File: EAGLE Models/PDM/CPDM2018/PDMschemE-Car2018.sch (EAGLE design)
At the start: 16 parts, among them Q1 PFETBS250

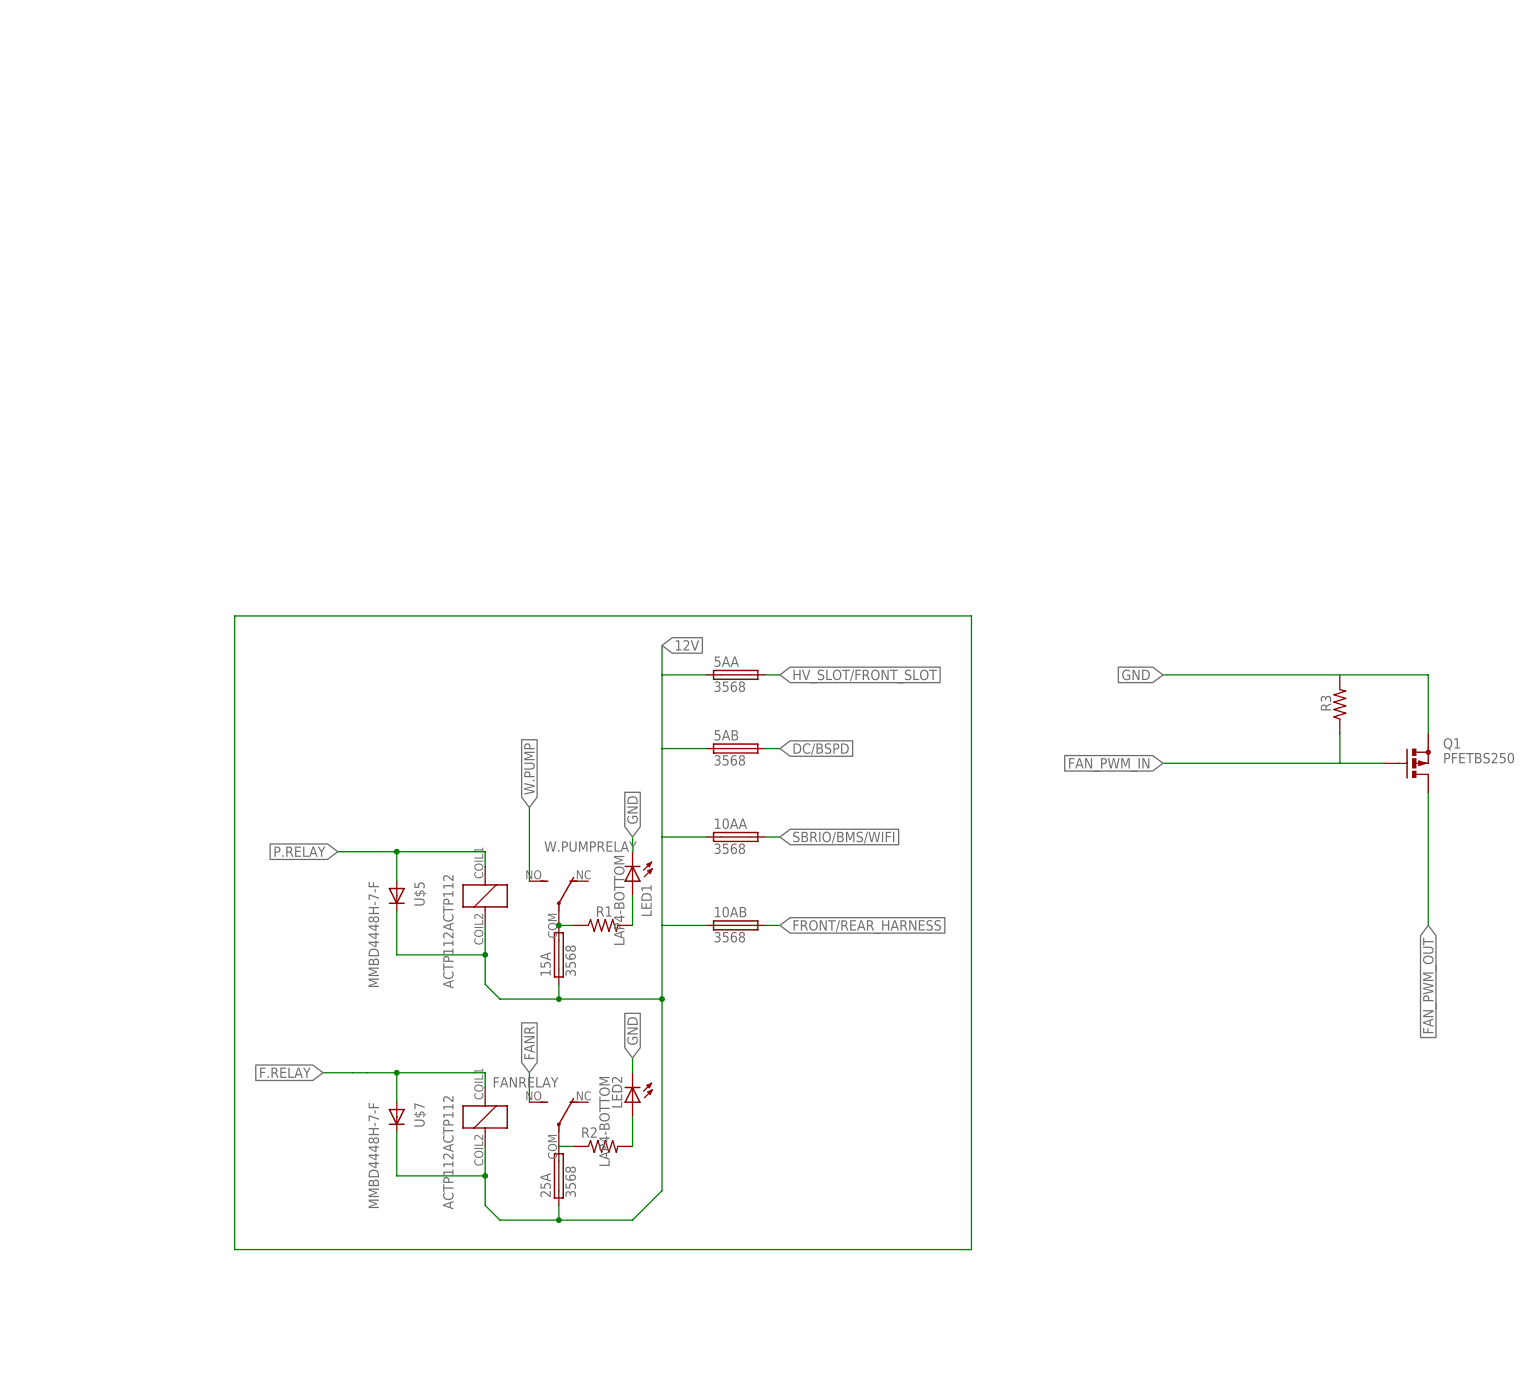
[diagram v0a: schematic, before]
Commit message: Organized PDM components
Organized PDM componenets into individualized boxes; Addded spacing for more readability
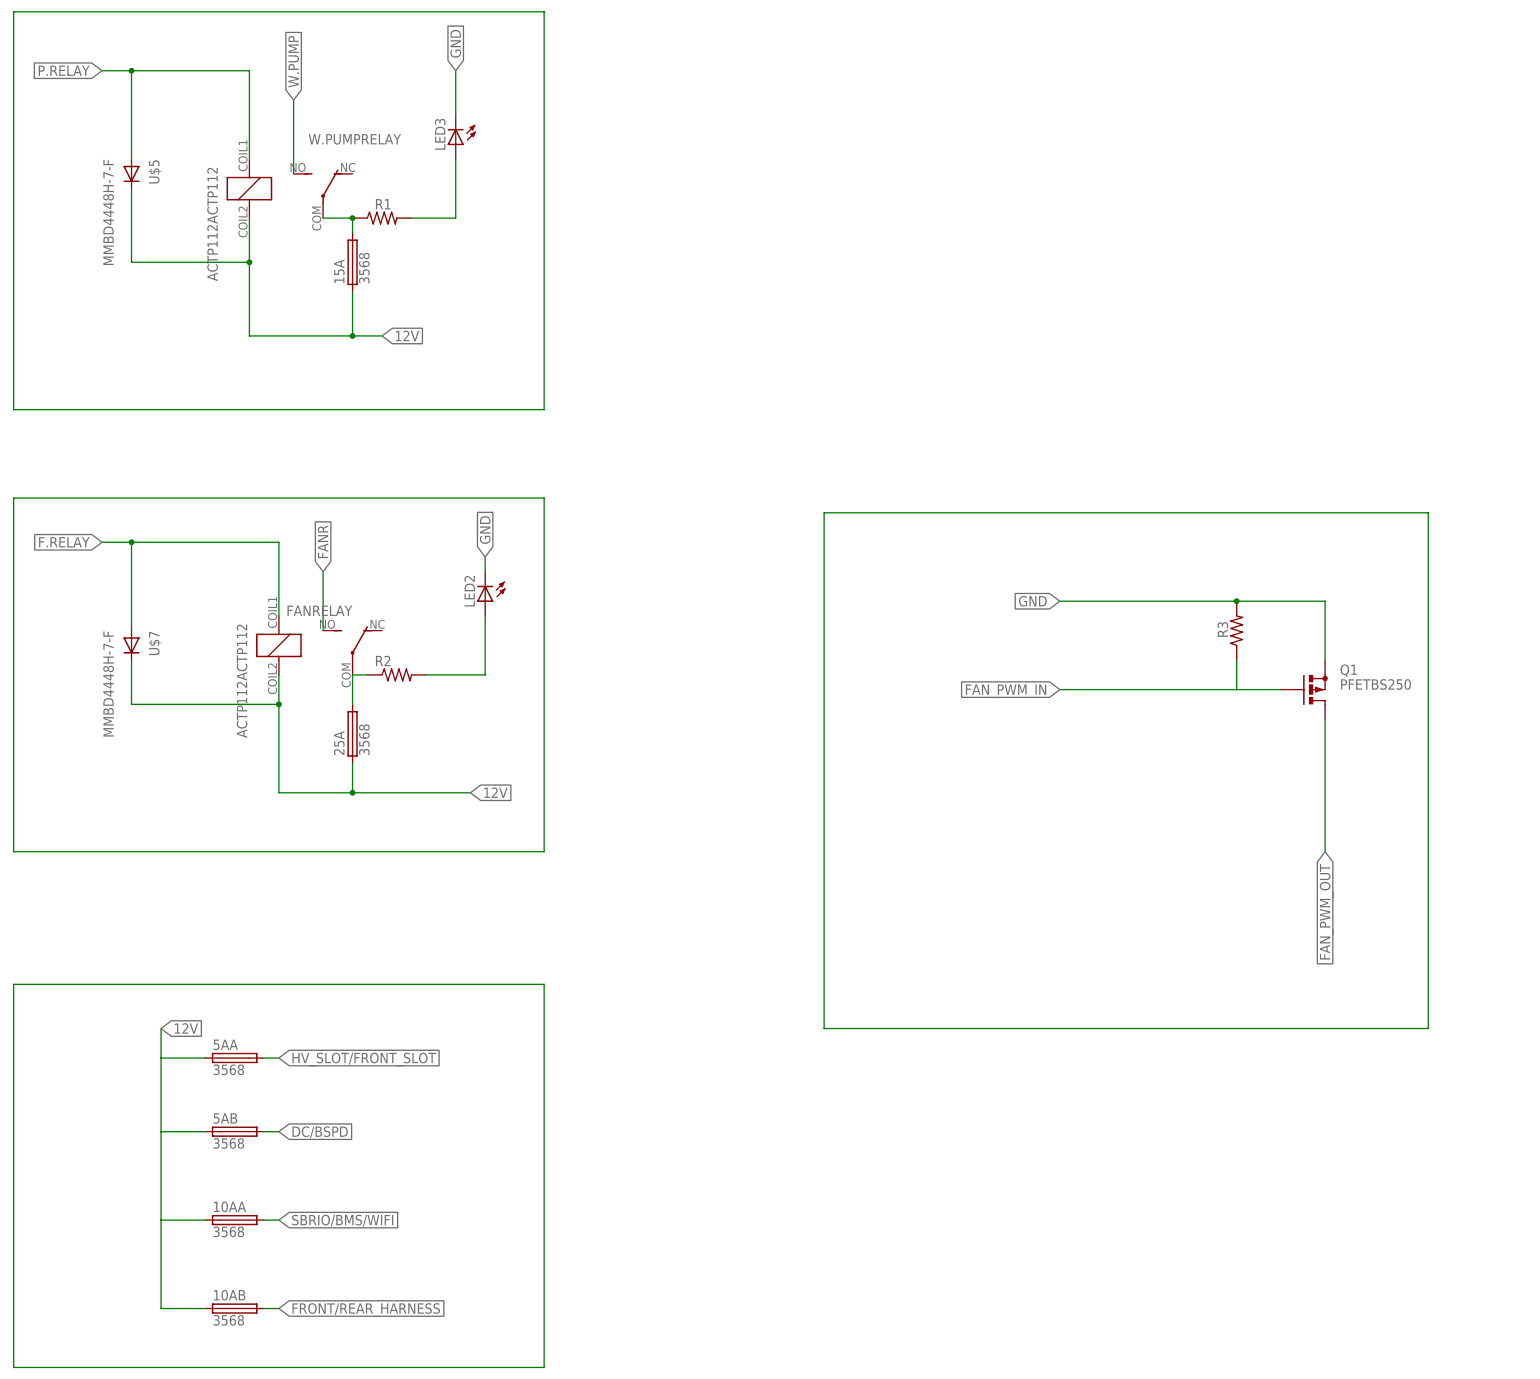
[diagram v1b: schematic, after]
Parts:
- removed LED1: LAP4-BOTTOM, led:LAP4-BOTTOM
- added LED3: (no value), adafruit:LEDCHIPLED_0805
- LED2: value LAP4-BOTTOM -> (none); device led:LAP4-BOTTOM -> adafruit:LEDCHIPLED_0805
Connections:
- net GND: now also LED3.C, R3.2; no longer LED1.C
- net N$1: now also LED3.A; no longer LED1.A
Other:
- moved on the sheet: 10AA, 10AB, 15A, 25A, 5AA, 5AB, FANRELAY, LED2, Q1, R1, R2, R3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

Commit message: E-Car PDM: Fuse Indicators added
The new type of blown fuse indicators were added. Organized circuit to be easier to read.
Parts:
- added D1, D2, D3, D4, D5, D6: 1N4004, adafruit:1N4004
- added LED1, LED4, LED5, LED6: (no value), adafruit:LEDCHIPLED_0805
- added Q2, Q3, Q4, Q5, Q6: 2N2907, adafruit:2N2907
- added R10, R12, R5, R6, R8: 47K, resistor:R-US_R1206
- added R11, R4, R7, R9: (no value), resistor:R-US_R1206
- added U$1: IRF40B207, infineon:IRF40B207
- Q1: value PFETBS250 -> 2N2907; device adafruit:PFETBS250 -> adafruit:2N2907
- R3: value (none) -> 47K
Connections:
- net FANR renamed FAN
- removed net FAN_PWM_IN: Q1.G, R3.1
- removed net FAN_PWM_OUT: Q1.D
- new net N$10: 15A.1, D1.A, W.PUMPRELAY.COM
- new net N$11: Q2.C, R4.1
- new net N$13: LED2.C, Q2.E
- new net N$14: D3.C, Q3.B, R6.1
- new net N$17: LED4.C, Q4.E
- new net N$18: D4.C, Q4.B, R8.1
- new net N$19: Q4.C, R7.1
- new net N$22: LED5.C, Q5.E
- new net N$23: D5.C, Q5.B, R10.1
- new net N$24: Q5.C, R9.1
- new net N$27: LED6.C, Q6.E
- new net N$28: D6.C, Q6.B, R12.1
- new net N$29: Q6.C, R11.1
- new net N$3: LED1.C, Q3.E
- new net N$5: Q1.C, R1.1
- net 12V: now also 10AA.2, 10AB.2, 15A.2, 25A.2, 5AA.2, 5AB.2, LED1.A, LED2.A, LED3.A, LED4.A, LED5.A, LED6.A; no longer 10AA.1, 10AB.1, 15A.1, 25A.1, 5AA.1, 5AB.1, FANRELAY.COIL2, U$5.C, U$7.C, W.PUMPRELAY.COIL2
- net DC/BSPD: now also 5AB.1, D4.A; no longer 5AB.2
- net F.RELAY: now also U$7.C; no longer U$7.A
- net FRONT/REAR_HARNESS: now also 10AB.1, D6.A; no longer 10AB.2
- net GND: now also FANRELAY.COIL2, R1.2, R10.2, R11.2, R12.2, R2.2, R4.2, R5.2, R6.2, R7.2, R8.2, R9.2, U$5.A, U$7.A, W.PUMPRELAY.COIL2; no longer LED2.C, LED3.C, Q1.S
- net HV_SLOT/FRONT_SLOT: now also 5AA.1, D3.A; no longer 5AA.2
- net N$1: now also LED3.C, Q1.E; no longer LED3.A, R1.2
- net N$2: now also Q3.C
- net N$4: now also 25A.1, D2.A, FANRELAY.COM; no longer LED2.A, R2.2
- net N$6: now also D1.C, Q1.B, R3.1; no longer 15A.2, R1.1, W.PUMPRELAY.COM
- net N$9: now also D2.C, Q2.B, R5.1; no longer 25A.2, FANRELAY.COM
- net P.RELAY: now also U$5.C; no longer U$5.A
- net SBRIO/BMS/WIFI: now also 10AA.1, D5.A; no longer 10AA.2
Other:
- note added: "Fan PWM MOSFET"
- note added: "Fan Relay w/ Blown Fuse Indicator"
- note added: "Non-Relayed Fuses /w Blown Fuse Indicator"
- note added: "Water Pump Relay w/ Blown Fuse Indicator"
- moved on the sheet: 10AA, 10AB, 15A, 25A, 5AA, 5AB, FANRELAY, LED2, LED3, R1, R2, R3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

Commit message: ECar - started board; fixed vals on schem
Added resistor values; need to fix packaging on the diodes. Starting on board after changes.
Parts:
- added R13: 47K, resistor:R-US_R1206
- R1, R11, R2, R4, R7, R9: value (none) -> 470
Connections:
- new net FAN_PWM_IN: R13.1, U$1.G
- new net FAN_PWM_OUT: U$1.D
- net GND: now also R13.2, U$1.S
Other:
- note added: "N-Channel MOSFET (Not a P-Channel)"
- moved on the sheet: U$1
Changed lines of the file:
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@@
 <part name="U$7" library="diodes-inc" deviceset="MMBD4448H-7-F" device=""/>
 <part name="25A" library="Keystone" deviceset="3568" device=""/>
-<part name="R1" library="resistor" library_urn="urn:adsk.eagle:library:348" deviceset="R-US_" device="R1206" package3d_urn="urn:adsk.eagle:package:26062/1"/>
+<part name="R1" library="resistor" library_urn="urn:adsk.eagle:library:348" deviceset="R-US_" device="R1206" package3d_urn="urn:adsk.eagle:package:26062/1" value="470"/>
 <part name="5AA" library="Keystone" deviceset="3568" device=""/>
 <part name="5AB" library="Keystone" deviceset="3568" device=""/>
@@
 <part name="R3" library="resistor" library_urn="urn:adsk.eagle:library:348" deviceset="R-US_" device="R1206" package3d_urn="urn:adsk.eagle:package:26062/1" value="47K"/>
 <part name="Q2" library="adafruit" deviceset="2N2907*" device=""/>
-<part name="R4" library="resistor" library_urn="urn:adsk.eagle:library:348" deviceset="R-US_" device="R1206" package3d_urn="urn:adsk.eagle:package:26062/1"/>
+<part name="R4" library="resistor" library_urn="urn:adsk.eagle:library:348" deviceset="R-US_" device="R1206" package3d_urn="urn:adsk.eagle:package:26062/1" value="470"/>
 <part name="R5" library="resistor" library_urn="urn:adsk.eagle:library:348" deviceset="R-US_" device="R1206" package3d_urn="urn:adsk.eagle:package:26062/1" value="47K"/>
 <part name="D2" library="adafruit" deviceset="1N4004" device=""/>
 <part name="Q3" library="adafruit" deviceset="2N2907*" device=""/>
-<part name="R2" library="resistor" library_urn="urn:adsk.eagle:library:348" deviceset="R-US_" device="R1206" package3d_urn="urn:adsk.eagle:package:26062/1"/>
+<part name="R2" library="resistor" library_urn="urn:adsk.eagle:library:348" deviceset="R-US_" device="R1206" package3d_urn="urn:adsk.eagle:package:26062/1" value="470"/>
 <part name="LED1" library="adafruit" deviceset="LED" device="CHIPLED_0805"/>
 <part name="R6" library="resistor" library_urn="urn:adsk.eagle:library:348" deviceset="R-US_" device="R1206" package3d_urn="urn:adsk.eagle:package:26062/1" value="47K"/>
@@
 <part name="LED4" library="adafruit" deviceset="LED" device="CHIPLED_0805"/>
 <part name="Q4" library="adafruit" deviceset="2N2907*" device=""/>
-<part name="R7" library="resistor" library_urn="urn:adsk.eagle:library:348" deviceset="R-US_" device="R1206" package3d_urn="urn:adsk.eagle:package:26062/1"/>
+<part name="R7" library="resistor" library_urn="urn:adsk.eagle:library:348" deviceset="R-US_" device="R1206" package3d_urn="urn:adsk.eagle:package:26062/1" value="470"/>
 <part name="R8" library="resistor" library_urn="urn:adsk.eagle:library:348" deviceset="R-US_" device="R1206" package3d_urn="urn:adsk.eagle:package:26062/1" value="47K"/>
 <part name="D4" library="adafruit" deviceset="1N4004" device=""/>
 <part name="LED5" library="adafruit" deviceset="LED" device="CHIPLED_0805"/>
 <part name="Q5" library="adafruit" deviceset="2N2907*" device=""/>
-<part name="R9" library="resistor" library_urn="urn:adsk.eagle:library:348" deviceset="R-US_" device="R1206" package3d_urn="urn:adsk.eagle:package:26062/1"/>
+<part name="R9" library="resistor" library_urn="urn:adsk.eagle:library:348" deviceset="R-US_" device="R1206" package3d_urn="urn:adsk.eagle:package:26062/1" value="470"/>
 <part name="R10" library="resistor" library_urn="urn:adsk.eagle:library:348" deviceset="R-US_" device="R1206" package3d_urn="urn:adsk.eagle:package:26062/1" value="47K"/>
 <part name="D5" library="adafruit" deviceset="1N4004" device=""/>
 <part name="LED6" library="adafruit" deviceset="LED" device="CHIPLED_0805"/>
 <part name="Q6" library="adafruit" deviceset="2N2907*" device=""/>
-<part name="R11" library="resistor" library_urn="urn:adsk.eagle:library:348" deviceset="R-US_" device="R1206" package3d_urn="urn:adsk.eagle:package:26062/1"/>
+<part name="R11" library="resistor" library_urn="urn:adsk.eagle:library:348" deviceset="R-US_" device="R1206" package3d_urn="urn:adsk.eagle:package:26062/1" value="470"/>
 <part name="R12" library="resistor" library_urn="urn:adsk.eagle:library:348" deviceset="R-US_" device="R1206" package3d_urn="urn:adsk.eagle:package:26062/1" value="47K"/>
 <part name="D6" library="adafruit" deviceset="1N4004" device=""/>
+<part name="R13" library="resistor" library_urn="urn:adsk.eagle:library:348" deviceset="R-US_" device="R1206" package3d_urn="urn:adsk.eagle:package:26062/1" value="47K"/>
 </parts>
 <sheets>
@@
 <wire x1="-68.58" y1="-96.52" x2="-68.58" y2="96.52" width="0.1524" layer="94"/>
 <text x="-66.04" y="91.44" size="1.778" layer="94">Non-Relayed Fuses /w Blown Fuse Indicator</text>
-<wire x1="198.12" y1="165.1" x2="322.58" y2="165.1" width="0.1524" layer="94"/>
-<wire x1="322.58" y1="165.1" x2="322.58" y2="86.36" width="0.1524" layer="94"/>
-<wire x1="322.58" y1="86.36" x2="198.12" y2="86.36" width="0.1524" layer="94"/>
-<wire x1="198.12" y1="86.36" x2="198.12" y2="165.1" width="0.1524" layer="94"/>
-<text x="200.66" y="160.02" size="1.778" layer="94">Fan PWM MOSFET</text>
+<wire x1="73.66" y1="187.96" x2="200.66" y2="187.96" width="0.1524" layer="94"/>
+<wire x1="200.66" y1="187.96" x2="200.66" y2="119.38" width="0.1524" layer="94"/>
+<wire x1="200.66" y1="119.38" x2="73.66" y2="119.38" width="0.1524" layer="94"/>
+<wire x1="73.66" y1="119.38" x2="73.66" y2="187.96" width="0.1524" layer="94"/>
+<text x="76.2" y="182.88" size="1.778" layer="94">Fan PWM MOSFET</text>
+<text x="139.7" y="154.94" size="1.778" layer="94">N-Channel MOSFET (Not a P-Channel)</text>
 </plain>
 <instances>
@@
 <instance part="LED2" gate="G$1" x="27.94" y="160.02"/>
 <instance part="LED3" gate="G$1" x="27.94" y="236.22"/>
-<instance part="U$1" gate="G$1" x="292.1" y="121.92"/>
+<instance part="U$1" gate="G$1" x="132.08" y="160.02"/>
 <instance part="Q1" gate="G$1" x="25.4" y="223.52"/>
 <instance part="D1" gate="1" x="10.16" y="233.68" rot="R270"/>
@@
 <attribute name="NAME" x="8.1026" y="-55.88" size="1.778" layer="95" rot="R180"/>
 <attribute name="VALUE" x="12.9286" y="-58.42" size="1.778" layer="96" rot="R180"/>
+</instance>
+<instance part="R13" gate="G$1" x="119.38" y="149.86" smashed="yes" rot="R270">
+<attribute name="NAME" x="120.8786" y="151.13" size="1.778" layer="95" rot="R270"/>
+<attribute name="VALUE" x="116.078" y="153.67" size="1.778" layer="96" rot="R270"/>
 </instance>
 </instances>
@@
 <junction x="5.08" y="-78.74"/>
 </segment>
+<segment>
+<pinref part="U$1" gate="G$1" pin="S"/>
+<wire x1="134.62" y1="154.94" x2="134.62" y2="139.7" width="0.1524" layer="91"/>
+<wire x1="134.62" y1="139.7" x2="119.38" y2="139.7" width="0.1524" layer="91"/>
+<pinref part="R13" gate="G$1" pin="2"/>
+<wire x1="119.38" y1="139.7" x2="119.38" y2="144.78" width="0.1524" layer="91"/>
+<label x="139.7" y="139.7" size="1.778" layer="95" xref="yes"/>
+<wire x1="139.7" y1="139.7" x2="134.62" y2="139.7" width="0.1524" layer="91"/>
+<junction x="134.62" y="139.7"/>
+</segment>
 </net>
 <net name="FAN_PWM_IN" class="0">
 <segment>
-<wire x1="254" y1="124.46" x2="243.84" y2="124.46" width="0.1524" layer="91"/>
-<label x="243.84" y="124.46" size="1.778" layer="95" rot="R180" xref="yes"/>
+<wire x1="119.38" y1="157.48" x2="109.22" y2="157.48" width="0.1524" layer="91"/>
+<label x="109.22" y="157.48" size="1.778" layer="95" rot="R180" xref="yes"/>
+<pinref part="R13" gate="G$1" pin="1"/>
+<wire x1="119.38" y1="154.94" x2="119.38" y2="157.48" width="0.1524" layer="91"/>
+<pinref part="U$1" gate="G$1" pin="G"/>
+<wire x1="119.38" y1="157.48" x2="129.54" y2="157.48" width="0.1524" layer="91"/>
+<junction x="119.38" y="157.48"/>
 </segment>
 </net>
 <net name="FAN_PWM_OUT" class="0">
 <segment>
-<wire x1="294.64" y1="134.62" x2="294.64" y2="144.78" width="0.1524" layer="91"/>
-<label x="294.64" y="144.78" size="1.778" layer="95" rot="R180" xref="yes"/>
-</segment>
-</net>
+<wire x1="134.62" y1="165.1" x2="134.62" y2="177.8" width="0.1524" layer="91"/>
+<label x="134.62" y="177.8" size="1.778" layer="95" xref="yes"/>
+<pinref part="U$1" gate="G$1" pin="D"/>
+</segment>
+</net>
